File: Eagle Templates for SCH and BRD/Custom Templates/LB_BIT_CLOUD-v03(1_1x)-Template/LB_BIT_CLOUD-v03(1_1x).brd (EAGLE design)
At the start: 27.2 x 57.8 mm, 17 parts, among them J2 BITSNAP_V03_MALE, J3 BITSNAP_V03_FEMALE, U1 LV321SOT23-5, U2 LV321SOT23-5

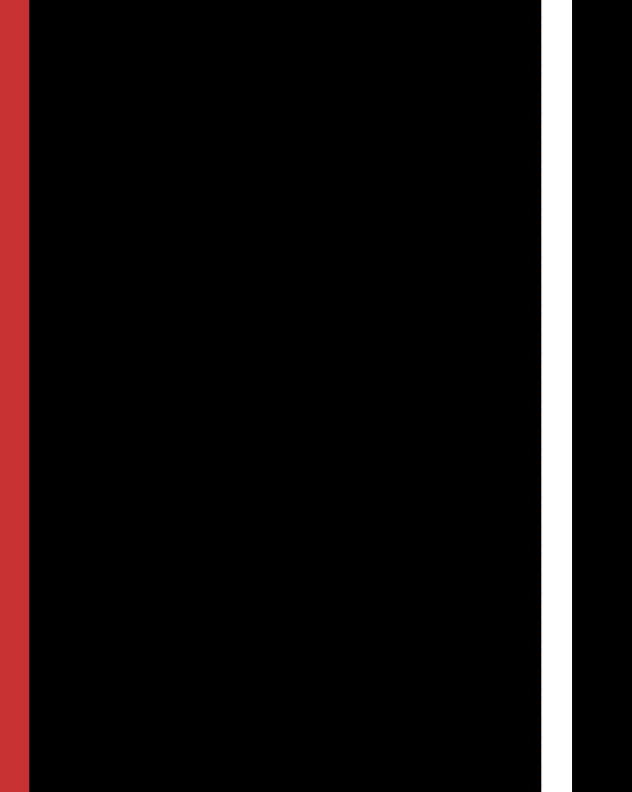
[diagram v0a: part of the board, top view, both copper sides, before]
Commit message: added bitlab logo and made minor changes to board templates. Updated littlebits library.
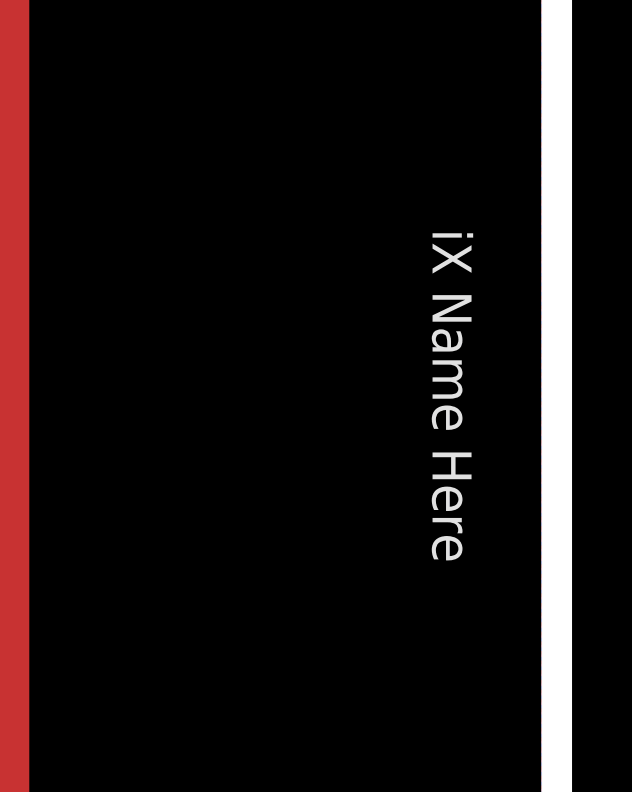
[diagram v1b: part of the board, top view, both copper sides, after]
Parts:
- added U$2: (no value), LITTLEBITS:BITLAB-LOGO
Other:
- board text added: "iX Name Here"
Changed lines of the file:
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@@
 <layer number="113" name="extra" color="10" fill="1" visible="yes" active="yes"/>
 <layer number="116" name="Patch_BOT" color="9" fill="4" visible="yes" active="yes"/>
+<layer number="118" name="Rect_Pads" color="7" fill="1" visible="no" active="yes"/>
 <layer number="121" name="_tsilk" color="7" fill="1" visible="yes" active="yes"/>
 <layer number="122" name="_bsilk" color="7" fill="1" visible="yes" active="yes"/>
@@
 <wire x1="-6.5" y1="58.94" x2="-6.5" y2="7.11" width="0" layer="20"/>
 <text x="-4.4" y="59.8" size="0.8128" layer="16" font="vector" ratio="12" rot="MR270">revX</text>
+<text x="16.7" y="33.025" size="1.3" layer="21" font="vector" rot="SR270" align="center">iX Name Here</text>
 </plain>
 <attributes>
@@
 <element name="U$1" library="ohw-logo" package="OSHW_FILLX150_NOTEXT" value="" x="14.2" y="55.8" rot="MR90"/>
 <element name="FRAME1" library="LITTLEBITS" package="FABDWG01-OHW" value="FRAME-LETTER" x="0" y="0"/>
+<element name="U$2" library="LITTLEBITS" package="BITLAB-LOGO" value="" x="15.2" y="37.1" rot="R270"/>
 </elements>
 <signals>

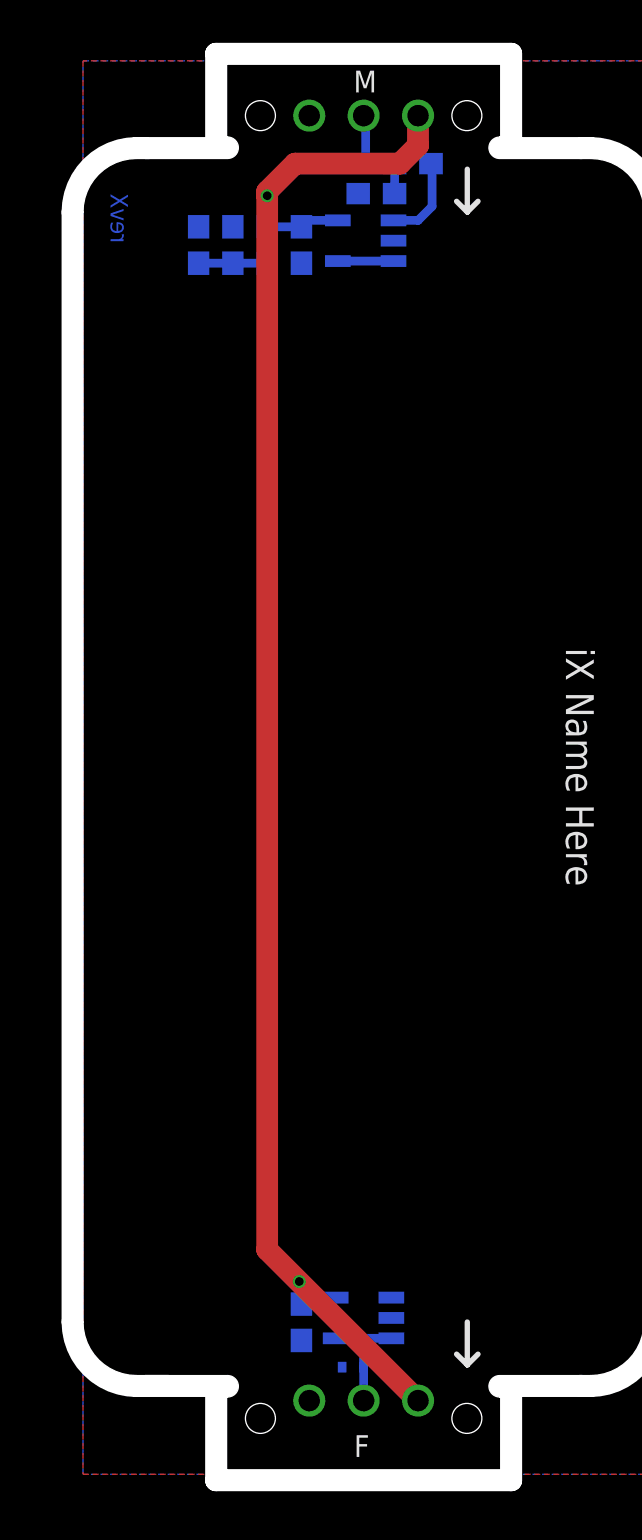
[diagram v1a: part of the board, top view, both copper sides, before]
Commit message: Updated templates
- Added ferrite beads
- Moved text and annotations off of Nets layer
- Minor layout changes
- Removed I/O/W prefix from reference designators
- Removed output stage components from output bits
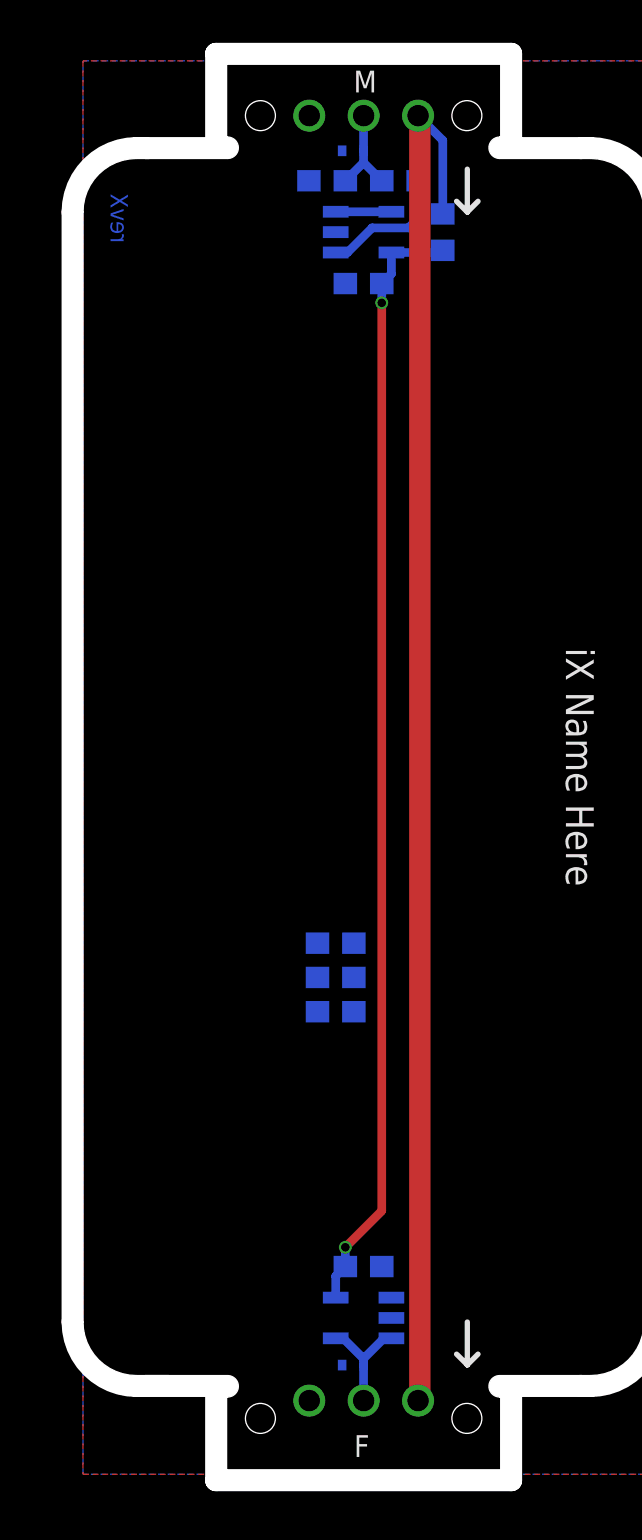
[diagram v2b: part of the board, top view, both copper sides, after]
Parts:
- removed I?C1: 0.1uF, LITTLEBITS:CAP-0603
- removed I?C2: 10uF, LITTLEBITS:CAP-0603
- removed I?C3: 1.0uF, LITTLEBITS:CAP-0603
- removed I?R1: 1meg, LITTLEBITS:RES-0603
- removed I?R2: 10K, LITTLEBITS:RES-0603
- removed I?R3, I?R4: 3K3, LITTLEBITS:RES-0603
- removed I?TVS1, I?TVS2: ESD9B5.0ST5G, LITTLEBITS:SOD-923
- added C1: 0.1uF, LITTLEBITS:CAP-0603
- added C2: 10uF, LITTLEBITS:CAP-0603
- added C3: 1.0uF, LITTLEBITS:CAP-0603
- added FB1: FERRITE-BEAD0603, LITTLEBITS:R0603
- added R1: 1meg, LITTLEBITS:RES-0603
- added R2: 10K, LITTLEBITS:RES-0603
- added R3, R4: 3K3, LITTLEBITS:RES-0603
- added TVS1, TVS2: ESD9B5.0ST5G, LITTLEBITS:SOD-923
- moved U1 0.41 mm to (6.60, 58.0), turned to 90 degrees
- renumbered J2 to BSM1, J3 to BSF1
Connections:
- removed net N$9: I?R2.1, U1.1
- new net LB_VCC: BSF1.VCC, BSM1.VCC1, FB1.2
- new net N$4: R2.1, U1.1
- net GND: now also C1.2, C2.2, C3.1, R1.1, R4.1, TVS1.1, TVS2.1; no longer I?C1.2, I?C2.2, I?C3.1, I?R1.1, I?R4.1, I?TVS1.1, I?TVS2.1
- net SIG_IN: now also R1.2, R2.2, TVS1.2; no longer I?R1.2, I?R2.2, I?TVS1.2
- net SIG_OUT: now also TVS2.2; no longer I?TVS2.2
- net VCC: now also C1.1, C3.2, FB1.1, R3.2; no longer BSF1.VCC, BSM1.VCC1, I?C1.1, I?C3.2, I?R3.2
- net VREF: now also C2.1, R3.1, R4.2; no longer I?C2.1, I?R3.1, I?R4.2
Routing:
- net LB_VCC: track 0.00 -> 65.0 mm, vias 0 -> 1
- net VCC: track 76.7 -> 52.3 mm
- net N$4: track 0.00 -> 6.26 mm
- net N$9: track 4.16 -> 0.00 mm
- net VREF: track 3.20 -> 0.00 mm
